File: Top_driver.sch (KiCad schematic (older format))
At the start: 7 parts, among them U3 6N137, U4 TC4420

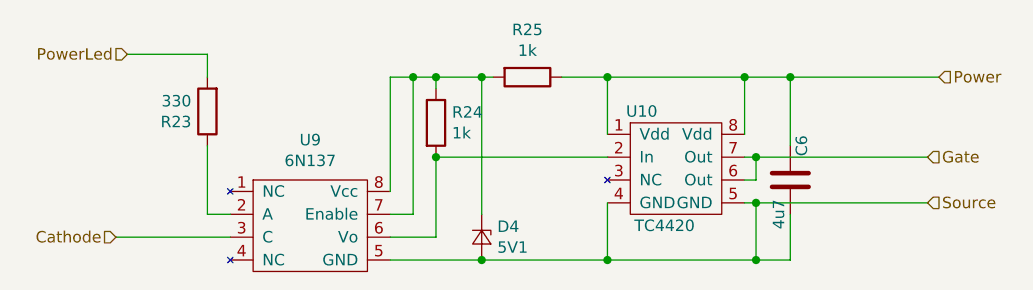
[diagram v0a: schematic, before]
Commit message: Separate drive connectors per phase
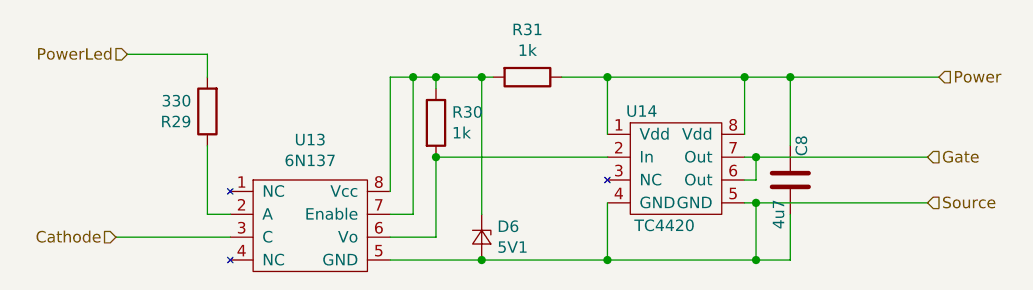
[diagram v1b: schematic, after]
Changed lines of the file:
@@
 AR Path="/5F647250/5F492C86" Ref="U12"  Part="1"
 AR Path="/5F64C514/5F492C86" Ref="U14"  Part="1"
-F 0 "U10" H 5800 3300 50  0000 C CNN
+F 0 "U14" H 5800 3300 50  0000 C CNN
 F 1 "TC4420" H 5900 2800 50  0000 C CNN
 F 2 "Package_DIP:DIP-8_W7.62mm_LongPads" H 5750 3050 50  0001 C CNN
@@
 AR Path="/5F647250/5F492C8D" Ref="C7"  Part="1"
 AR Path="/5F64C514/5F492C8D" Ref="C8"  Part="1"
-F 0 "C6" V 6400 2950 50  0000 C CNN
+F 0 "C8" V 6400 2950 50  0000 C CNN
 F 1 "4u7" V 6500 3250 50  0000 C CNN
 F 2 "Capacitor_SMD:C_0805_2012Metric" H 6488 2950 50  0001 C CNN
@@
 AR Path="/5F647250/5F492CA0" Ref="U11"  Part="1"
 AR Path="/5F64C514/5F492CA0" Ref="U13"  Part="1"
-F 0 "U9" H 4350 3375 50  0000 C CNN
+F 0 "U13" H 4350 3375 50  0000 C CNN
 F 1 "6N137" H 4350 3284 50  0000 C CNN
 F 2 "Package_DIP:DIP-8_W7.62mm_LongPads" H 4100 3000 50  0001 C CNN
@@
 AR Path="/5F647250/5F492CAF" Ref="R26"  Part="1"
 AR Path="/5F64C514/5F492CAF" Ref="R29"  Part="1"
-F 0 "R23" H 3970 2846 50  0000 L CNN
+F 0 "R29" H 3970 2846 50  0000 L CNN
 F 1 "330" H 3970 2755 50  0000 L CNN
 F 2 "Resistor_SMD:R_0805_2012Metric" V 3830 2800 50  0001 C CNN
@@
 AR Path="/5F647250/5F4943B6" Ref="R28"  Part="1"
 AR Path="/5F64C514/5F4943B6" Ref="R31"  Part="1"
-F 0 "R25" V 5093 2650 50  0000 C CNN
+F 0 "R31" V 5093 2650 50  0000 C CNN
 F 1 "1k" V 5184 2650 50  0000 C CNN
 F 2 "Resistor_SMD:R_0805_2012Metric" V 5230 2650 50  0001 C CNN
@@
 AR Path="/5F647250/5F494F6C" Ref="D5"  Part="1"
 AR Path="/5F64C514/5F494F6C" Ref="D6"  Part="1"
-F 0 "D4" V 5054 3418 50  0000 L CNN
+F 0 "D6" V 5054 3418 50  0000 L CNN
 F 1 "5V1" V 5145 3418 50  0000 L CNN
 F 2 "Diode_SMD:D_MiniMELF" V 5100 3350 50  0001 C CNN
@@
 AR Path="/5F647250/5F495096" Ref="R27"  Part="1"
 AR Path="/5F64C514/5F495096" Ref="R30"  Part="1"
-F 0 "R24" H 4970 2896 50  0000 L CNN
+F 0 "R30" H 4970 2896 50  0000 L CNN
 F 1 "1k" H 4970 2805 50  0000 L CNN
 F 2 "Resistor_SMD:R_0805_2012Metric" V 4830 2850 50  0001 C CNN
